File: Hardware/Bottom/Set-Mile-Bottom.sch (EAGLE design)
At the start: 7 parts, among them U1 NRF52840_MDBT50

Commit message: updated board design to section 2
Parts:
- removed C1, C2: (no value), LinnesLab-Passives:CAPACITOR0603
- removed CORTEX2: CORTEX_DEBUG_PTH, LinnesLab-Connectors:CORTEX_DEBUG_PTH
- removed L1: 10u, LinnesLab-Passives:INDUCTOR0603
- removed SW2: (no value), LinnesLab-Switches:SPST-PTS830GG140-COPY.1-3
- removed XTAL1: 32.768kHz, LinnesLab-Clocks:CRYSTALECS-.327-12.5-12-C-TR
- added C10, C11, C17, C18, C22, C24: 100n, LinnesLab-Passives:CAPACITOR0603
- added C14, C19: 2.2n, LinnesLab-Passives:CAPACITOR0603
- added C15, C16: 2.2u, LinnesLab-Passives:CAPACITOR0603
- added C20: 22u, LinnesLab-Passives:CAPACITOR0603
- added C21: 22n, LinnesLab-Passives:CAPACITOR0603
- added IMU1: LSM6DS3_CAST, LinnesLab-Sensors:LSM6DS3_CAST
- added J1: (no value), LinnesLab-Connectors:CONN_07
- added OP3: (no value), LinnesLab-AnalogIC:OP-QUAD-SO14
- added OP4: (no value), LinnesLab-AnalogIC:OP-SINGLEOT
- added Q1: (no value), LinnesLab-DiscreteSemi:NPN-GENERIC
- added R13, R15, R19, R21: 220k, LinnesLab-Passives:RESISTOR0603
- added R14, R22: 10M, LinnesLab-Passives:RESISTOR0603
- added R16: (no value), LinnesLab-Passives:RESISTOR0603
- added R17, R18: 10k, LinnesLab-Passives:RESISTOR0402
- added R20, R23: 1M, LinnesLab-Passives:RESISTOR0603
- added R24: 10k, LinnesLab-Passives:RESISTOR0603
- added U$3: (no value), LinnesLab-Connectors:PPG.MODULE.2
- added U$4: AD5171, LinnesLab-DigitalIC:AD5171
- U1: value NRF52840_MDBT50 -> AD5242-SO16; device LinnesLab-Microcontrollers:NRF52840_MDBT50 -> LinnesLab-DigitalIC:AD5242-SO16
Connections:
- removed net A0: U1.P0.04/AIN2
- removed net A1: U1.P0.05/AIN3
- removed net A2: U1.P0.30/AIN6
- removed net A3: U1.P0.28/AIN4
- removed net A4: U1.P0.02/AIN0
- removed net A5: U1.P0.03/AIN1
- removed net AREF: U1.P0.31/AIN7
- removed net D10: U1.P0.27
- removed net D11: U1.P0.06
- removed net D12: U1.P0.08
- removed net D13: U1.P1.09
- removed net D2: U1.P0.10/NFC2
- removed net D5: U1.P1.08
- removed net D6: U1.P0.07
- removed net D9: U1.P0.26
- removed net DCCH: L1.2, U1.DCCH
- removed net LED1: U1.P1.15
- removed net LED2: U1.P1.10
- removed net MISO: U1.P0.15
- removed net MOSI: U1.P0.13
- removed net N$3: C2.2, U1.P0.00/XL1, XTAL1.2
- removed net NEOPIX: U1.P0.16
- removed net QSPI_CS: U1.P0.20
- removed net QSPI_DATA0: U1.P0.17
- removed net QSPI_DATA1: U1.P0.22
- removed net QSPI_DATA2: U1.P0.23
- removed net QSPI_DATA3: U1.P0.21
- removed net QSPI_SCK: U1.P0.19
- removed net RESET: CORTEX2.!RESET, SW2.B, U1.P0.18/RESET
- removed net RXD: U1.P0.24
- removed net SCK: U1.P0.14
- removed net SWCLK: CORTEX2.SWDCLK/TCK, U1.SWDCLK
- removed net SWDIO: CORTEX2.SWDIO/TMS, U1.SWDIO
- removed net SWITCH: U1.P1.02
- removed net SWO: CORTEX2.SWO/TDO, U1.P1.00
- removed net TXD: U1.P0.25
- removed net USBD+: U1.D+
- removed net USBD-: U1.D-
- removed net VDIV: U1.P0.29/AIN5
- removed net V_USB: U1.VBUS
- new net A6/TIA: C10.2, C15.1, J1.7, OP4G$1.OUT, U1.W1
- new net A7/PPG: C21.2, J1.5, OP3G$1.OUT, U1.B2
- new net D29/LED.CTRL: J1.6, U$4.A
- new net G.A1: U1.A1
- new net G.A2: U1.A2
- new net G.O1: U1.O1
- new net G.O2: U1.O2
- new net G.W2: C21.1, OP3G$1.-IN, R24.1, U1.W2
- new net LED.C: Q1.C, U$3.LD1.C
- new net N$10: OP3G$4.+IN, R17.1, R18.2
- new net N$13: C15.2, OP3G$2.+IN, R13.1, R19.2
- new net N$15: C14.2, OP3G$2.-IN, R14.1, R20.2
- new net N$16: C14.1, C16.1, OP3G$2.OUT, R14.2
- new net N$17: C16.2, OP3G$3.+IN, R15.1, R21.2
- new net N$18: C19.2, OP3G$3.-IN, R22.1, R23.2
- new net N$19: C19.1, C20.1, OP3G$3.OUT, R22.2
- new net N$20: C20.2, R24.2
- new net N$4: J1.4
- new net N$7: J1.1
- new net N$8: Q1.B, R16.2
- new net N$9: R16.1, U$4.B, U$4.W
- new net PD.C: C10.1, OP4G$1.-IN, U$3.PD.C, U1.B1
- new net VREF: OP3G$1.+IN, OP3G$4.-IN, OP3G$4.OUT, R20.1, R23.1
- net 3.3V: now also C11.2, C17.2, C18.2, C22.2, C24.2, IMU1.VCC, OP3G$5.V+, OP4G$2.V+, R13.2, R15.2, R17.2, U$3.V+, U$4.A0, U$4.VDD, U1.!SHDN; no longer CORTEX2.VCC, L1.1, U1.VDDH
- net GND: now also C11.1, C17.1, C18.1, C22.1, C24.1, IMU1.GND, OP3G$5.V-, OP4G$1.+IN, OP4G$2.V-, Q1.E, R18.1, R19.1, R21.1, U$3.GND, U$4.GND, U1.AD0, U1.AD1, U1.DGND, U1.VSS; no longer C1.2, C2.1, CORTEX2.GND@3, CORTEX2.GND@5, CORTEX2.GNDDTCT, CORTEX2.KEY, SW2.A, U1.GND@1, U1.GND@15, U1.GND@2, U1.GND@33, U1.GND@55
- net N$5: now also J1.3; no longer C1.1, U1.P0.01/XL2, XTAL1.1
- net N$6: now also J1.2; no longer CORTEX2.NC/TDI
- net SCL: now also IMU1.SCL, U$4.SCL, U1.SCL; no longer U1.P0.11
- net SDA: now also IMU1.SDA, U$4.SDA, U1.SDA; no longer U1.P0.12
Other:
- note added: "Active Bandpass Filters"
- note added: "Digital Potentiometers"
- note added: "I2C Address: 0x2C"
- note added: "I2C Address: 0x2D"
- note added: "Photodiode and LEDs"
- note added: "Transimpedance Amplifier"
- note removed: "Reset Button"

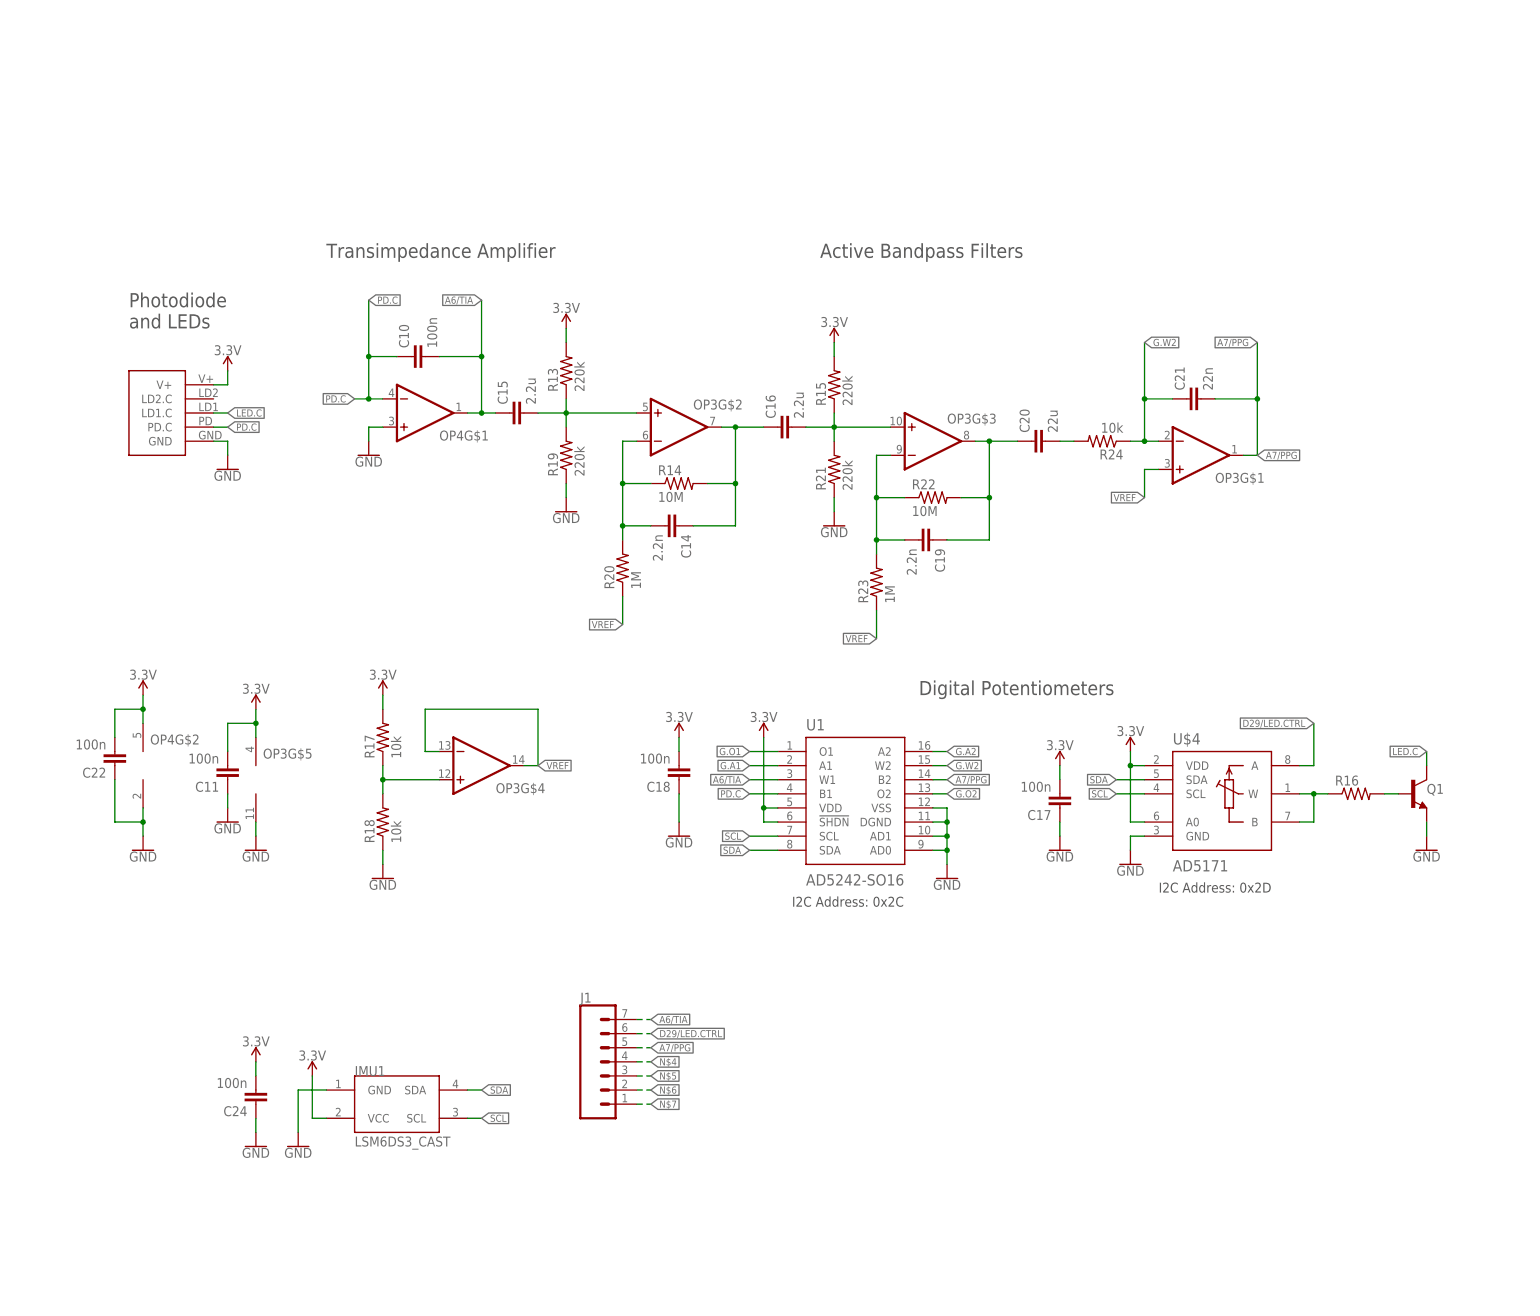
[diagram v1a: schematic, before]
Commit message: routing bottom board and oranized top board
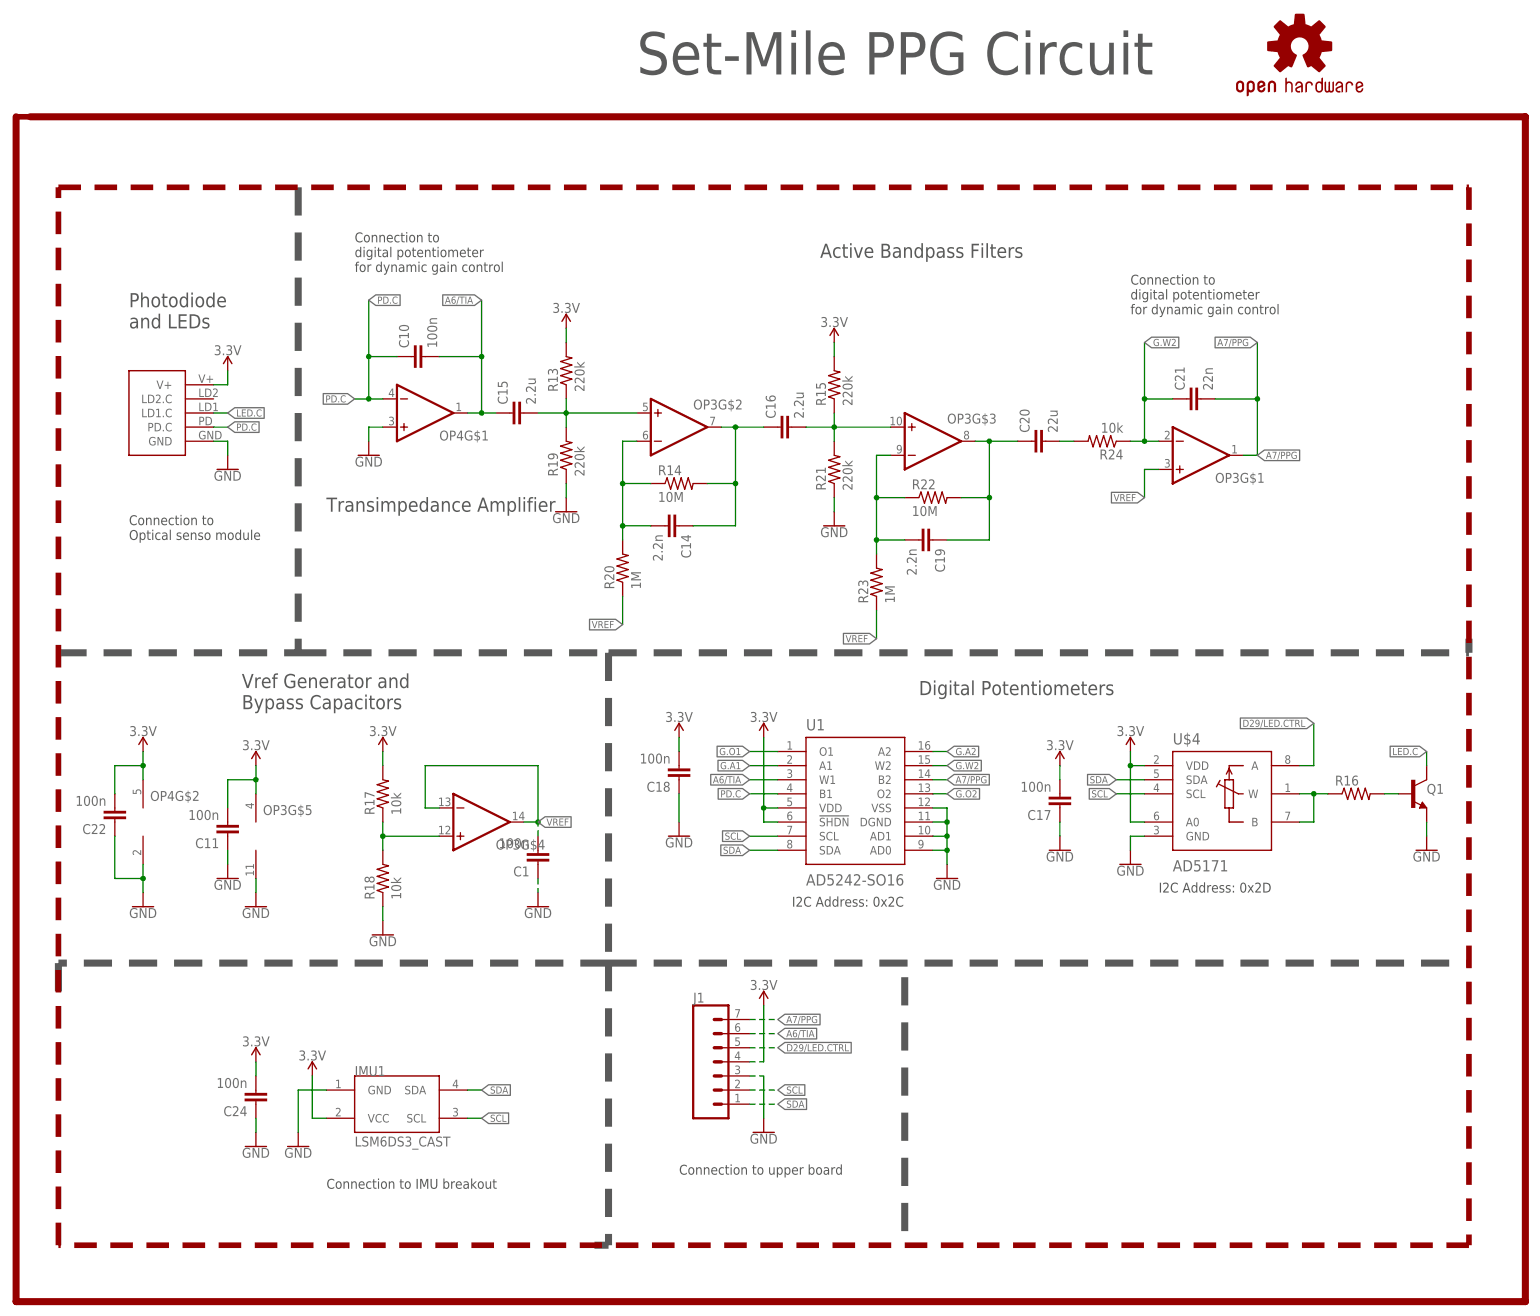
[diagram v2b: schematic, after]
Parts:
- added C1: 100n, LinnesLab-Passives:CAPACITOR0603
- added LOGO1: REVISION.A, LinnesLab-Logos:REVISION.A
- added LOGO2: OSHW-LOGOL, LinnesLab-Logos:OSHW-LOGOL
- J1: device LinnesLab-Connectors:CONN_07 -> LinnesLab-Connectors:CONN_07-1.27MM
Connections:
- removed net N$4: J1.4
- removed net N$5: J1.3
- removed net N$6: J1.2
- removed net N$7: J1.1
- net 3.3V: now also J1.4
- net A6/TIA: now also J1.6; no longer J1.7
- net A7/PPG: now also J1.7; no longer J1.5
- net D29/LED.CTRL: now also J1.5; no longer J1.6
- net GND: now also C1.1, J1.3
- net SCL: now also J1.2
- net SDA: now also J1.1
- net VREF: now also C1.2
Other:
- note added: "Connection to IMU breakout"
- note added: "Connection to Optical senso module"
- note added: "Connection to digital potentiometer for dynamic gain control"
- note added: "Connection to upper board"
- note added: "Set-Mile PPG Circuit"
- note added: "Vref Generator and Bypass Capacitors"
- moved on the sheet: C11, C22, J1, OP3G$4, OP3G$5, OP4G$2, R17, R18
